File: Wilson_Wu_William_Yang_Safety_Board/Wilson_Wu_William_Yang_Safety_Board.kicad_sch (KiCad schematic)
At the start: 46 parts, among them J1 22035035, J4 M22-7130442, Q5 IRLML6344TRPBF, U1 STM32, U11 LMV331IDBVR, U2 MCP2562-E_P, U3 10kohm, U4 SN74HCS21QPWRQ1

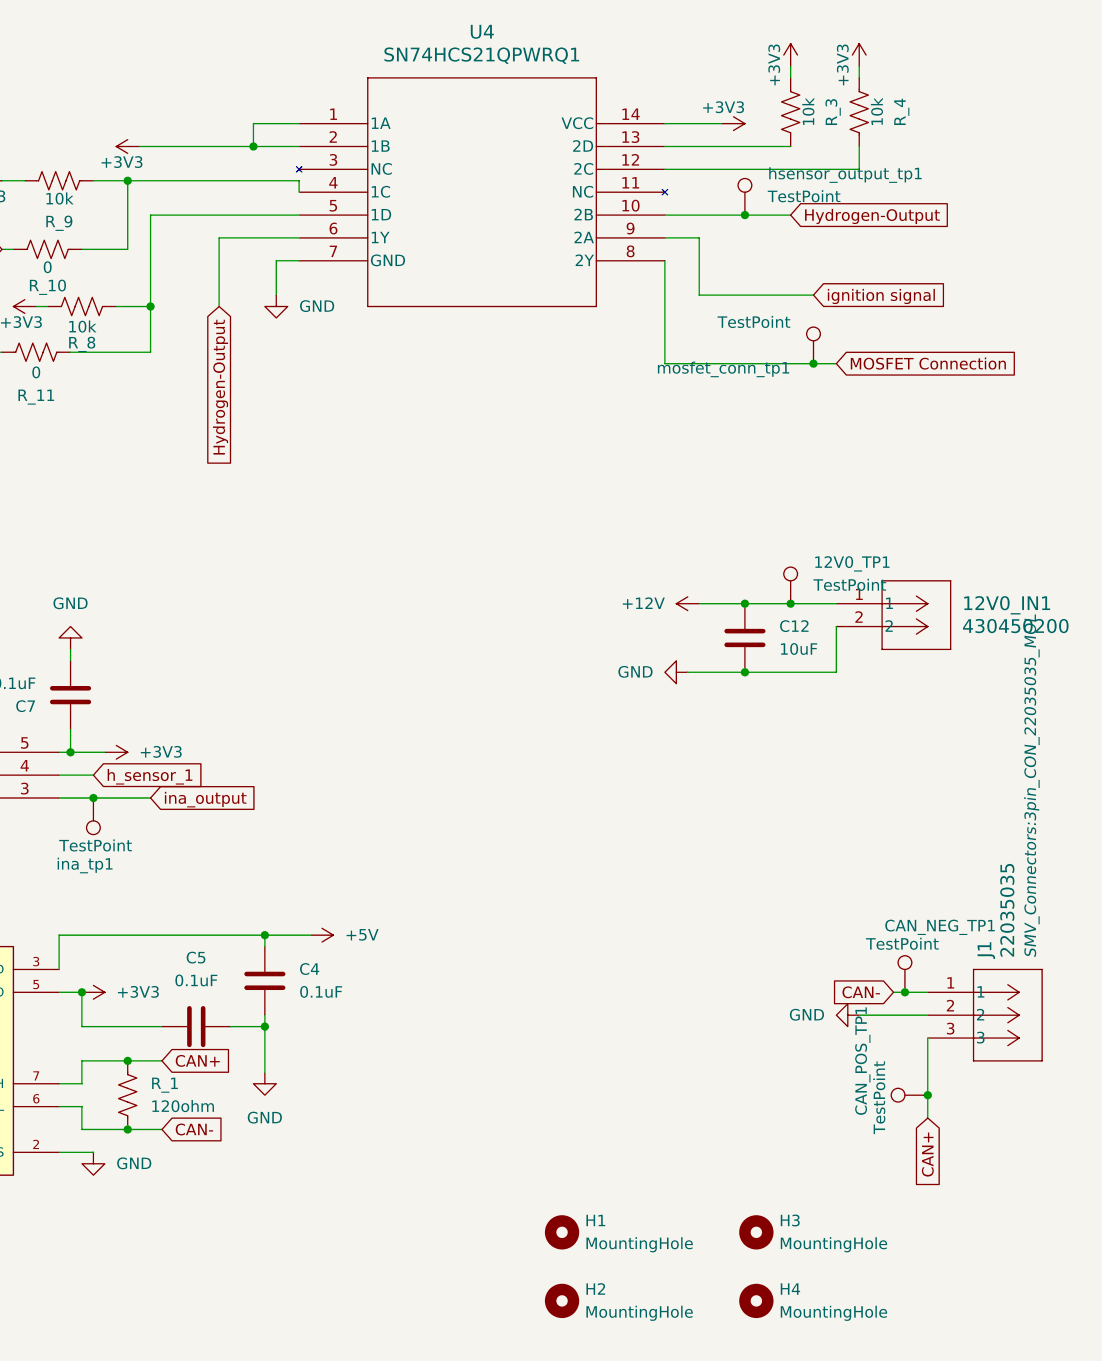
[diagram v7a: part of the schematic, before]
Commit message: feedback from soloman
made routing further from pads, swapped canl and canh, and added more stitching
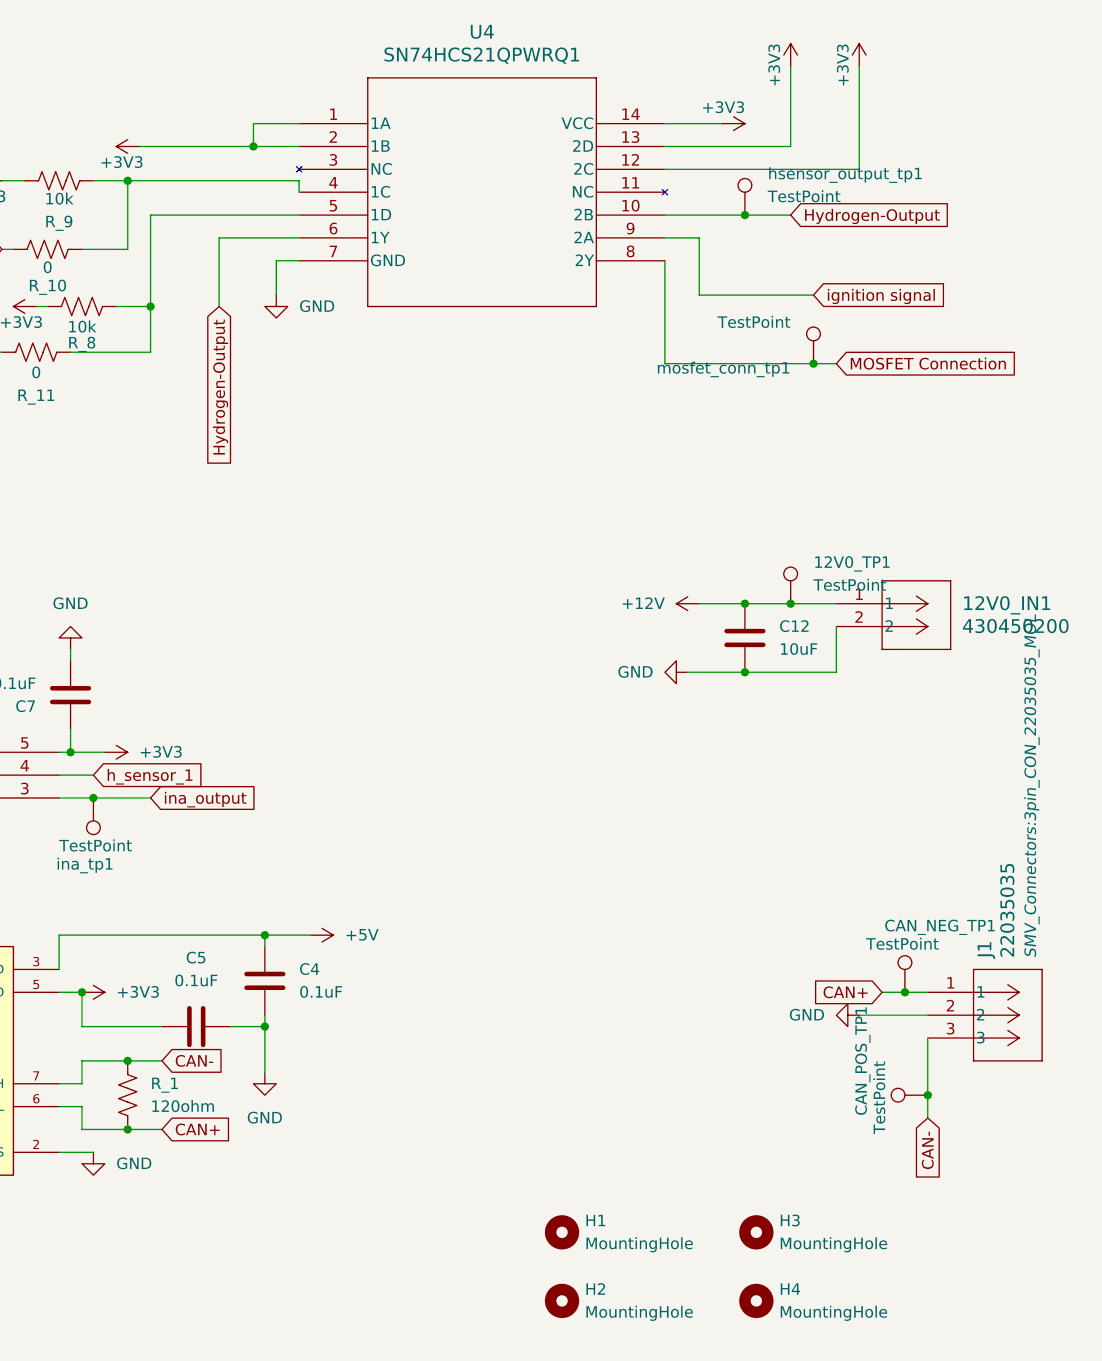
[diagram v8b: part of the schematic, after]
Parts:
- removed R_3, R_4: 10k, Resistor_SMD:R_0805_2012Metric, symbol Device:R_US
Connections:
- net +3V3: now also U4.12 (2C), U4.13 (2D)
- net CAN+: now also CAN_NEG_TP1.1, J1.1, R_1.2, U2.6 (CANL); no longer CAN_POS_TP1.1, J1.3, R_1.1, U2.7 (CANH)
- net CAN-: now also CAN_POS_TP1.1, J1.3, R_1.1, U2.7 (CANH); no longer CAN_NEG_TP1.1, J1.1, R_1.2, U2.6 (CANL)
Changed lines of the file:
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@@
 	(wire
 		(pts
-			(xy 262.89 17.78) (xy 262.89 19.05)
-		)
-		(stroke
-			(width 0)
-			(type default)
-		)
-	)
-	(wire
-		(pts
 			(xy -13.97 189.23) (xy -12.7 189.23)
 		)
@@
 	(wire
 		(pts
-			(xy 262.89 26.67) (xy 262.89 29.21)
+			(xy 262.89 17.78) (xy 262.89 29.21)
 		)
 		(stroke
@@
 	(wire
 		(pts
-			(xy 266.7 120.65) (xy 267.97 120.65)
+			(xy 265.43 120.65) (xy 267.97 120.65)
 		)
 		(stroke
@@
 	(wire
 		(pts
-			(xy 255.27 17.78) (xy 255.27 19.05)
+			(xy 255.27 17.78) (xy 255.27 26.67)
 		)
 		(stroke
@@
 		)
 	)
-	(global_label "CAN+"
-		(shape input)
-		(at 185.42 128.27 0)
-		(fields_autoplaced yes)
-		(effects
-			(font
-				(size 1.27 1.27)
-			)
-			(justify left)
-		)
-		(property "Intersheetrefs" "${INTERSHEET_REFS}"
-			(at 193.6667 128.27 0)
-			(effects
-				(font
-					(size 1.27 1.27)
-				)
-				(justify left)
-				(hide yes)
-			)
-		)
-	)
 	(global_label "optocoupler-output"
 		(shape input)
@@
 	(global_label "CAN-"
 		(shape input)
+		(at 270.51 134.62 270)
+		(fields_autoplaced yes)
+		(effects
+			(font
+				(size 1.27 1.27)
+			)
+			(justify right)
+		)
+		(property "Intersheetrefs" "${INTERSHEET_REFS}"
+			(at 270.51 142.8667 90)
+			(effects
+				(font
+					(size 1.27 1.27)
+				)
+				(justify right)
+				(hide yes)
+			)
+		)
+	)
+	(global_label "CAN+"
+		(shape input)
 		(at 185.42 135.89 0)
 		(fields_autoplaced yes)
@@
 		)
 	)
-	(global_label "CAN+"
+	(global_label "Hydrogen-Output"
 		(shape input)
-		(at 270.51 134.62 270)
+		(at 191.77 44.45 270)
 		(fields_autoplaced yes)
 		(effects
@@
 		)
 		(property "Intersheetrefs" "${INTERSHEET_REFS}"
-			(at 270.51 142.8667 90)
+			(at 191.77 64.0054 90)
 			(effects
 				(font
@@
 		)
 	)
-	(global_label "Hydrogen-Output"
+	(global_label "CAN+"
 		(shape input)
-		(at 191.77 44.45 270)
+		(at 265.43 120.65 180)
 		(fields_autoplaced yes)
 		(effects
@@
 		)
 		(property "Intersheetrefs" "${INTERSHEET_REFS}"
-			(at 191.77 64.0054 90)
+			(at 257.1833 120.65 0)
 			(effects
 				(font
@@
 		)
 	)
-	(global_label "Hydrogen-Output"
+	(global_label "CAN-"
 		(shape input)
-		(at 29.21 156.21 180)
+		(at 185.42 128.27 0)
 		(fields_autoplaced yes)
 		(effects
@@
 				(size 1.27 1.27)
 			)
-			(justify right)
+			(justify left)
 		)
 		(property "Intersheetrefs" "${INTERSHEET_REFS}"
-			(at 9.6546 156.21 0)
+			(at 193.6667 128.27 0)
 			(effects
 				(font
 					(size 1.27 1.27)
 				)
-				(justify right)
+				(justify left)
 				(hide yes)
 			)
 		)
 	)
-	(global_label "CAN-"
+	(global_label "Hydrogen-Output"
 		(shape input)
-		(at 266.7 120.65 180)
+		(at 29.21 156.21 180)
 		(fields_autoplaced yes)
 		(effects
@@
 		)
 		(property "Intersheetrefs" "${INTERSHEET_REFS}"
-			(at 258.4533 120.65 0)
+			(at 9.6546 156.21 0)
 			(effects
 				(font
@@
 	)
 	(symbol
-		(lib_id "Device:R_US")
-		(at 255.27 22.86 0)
-		(unit 1)
-		(exclude_from_sim no)
-		(in_bom yes)
-		(on_board yes)
-		(dnp no)
-		(property "Reference" "R_3"
-			(at 259.842 22.86 90)
-			(effects
-				(font
-					(size 1.27 1.27)
-				)
-			)
-		)
-		(property "Value" "10k"
-			(at 257.302 22.86 90)
-			(effects
-				(font
-					(size 1.27 1.27)
-				)
-			)
-		)
-		(property "Footprint" "Resistor_SMD:R_0805_2012Metric"
-			(at 256.286 23.114 90)
-			(effects
-				(font
-					(size 1.27 1.27)
-				)
-				(hide yes)
-			)
-		)
-		(property "Datasheet" "~"
-			(at 255.27 22.86 0)
-			(effects
-				(font
-					(size 1.27 1.27)
-				)
-				(hide yes)
-			)
-		)
-		(property "Description" "Resistor, US symbol"
-			(at 255.27 22.86 0)
-			(effects
-				(font
-					(size 1.27 1.27)
-				)
-				(hide yes)
-			)
-		)
-		(pin "1"
-		)
-		(pin "2"
-		)
-		(instances
-			(project "Wilson_Wu_William_Yang_Safety_Board"
-				(path "/fa857c32-0741-4b91-b122-1a57686bb514"
-					(reference "R_3")
-					(unit 1)
-				)
-			)
-		)
-	)
-	(symbol
 		(lib_id "power:GND")
 		(at 36.83 90.17 0)
@@
 					(unit 1)
 				)
-			)
-		)
-	)
-	(symbol
-		(lib_id "Device:R_US")
-		(at 262.89 22.86 0)
-		(unit 1)
-		(exclude_from_sim no)
-		(in_bom yes)
-		(on_board yes)
-		(dnp no)
-		(property "Reference" "R_4"
-			(at 267.462 22.86 90)
-			(effects
-				(font
-					(size 1.27 1.27)
-				)
-			)
-		)
-		(property "Value" "10k"
-			(at 264.922 22.86 90)
-			(effects
-				(font
-					(size 1.27 1.27)
-				)
-			)
-		)
-		(property "Footprint" "Resistor_SMD:R_0805_2012Metric"
-			(at 263.906 23.114 90)
-			(effects
-				(font
-					(size 1.27 1.27)
-				)
-				(hide yes)
-			)
-		)
-		(property "Datasheet" "~"
-			(at 262.89 22.86 0)
-			(effects
-				(font
-					(size 1.27 1.27)
-				)
-				(hide yes)
-			)
-		)
-		(property "Description" "Resistor, US symbol"
-			(at 262.89 22.86 0)
-			(effects
-				(font
-					(size 1.27 1.27)
-				)
-				(hide yes)
-			)
-		)
-		(pin "1"
-		)
-		(pin "2"
-		)
-		(instances
-			(project "Wilson_Wu_William_Yang_Safety_Board"
-				(path "/fa857c32-0741-4b91-b122-1a57686bb514"
-					(reference "R_4")
-					(unit 1)
-				)
